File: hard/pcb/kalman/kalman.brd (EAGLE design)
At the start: 84 x 65 mm, 89 parts, among them X1 USB-SMD-NS

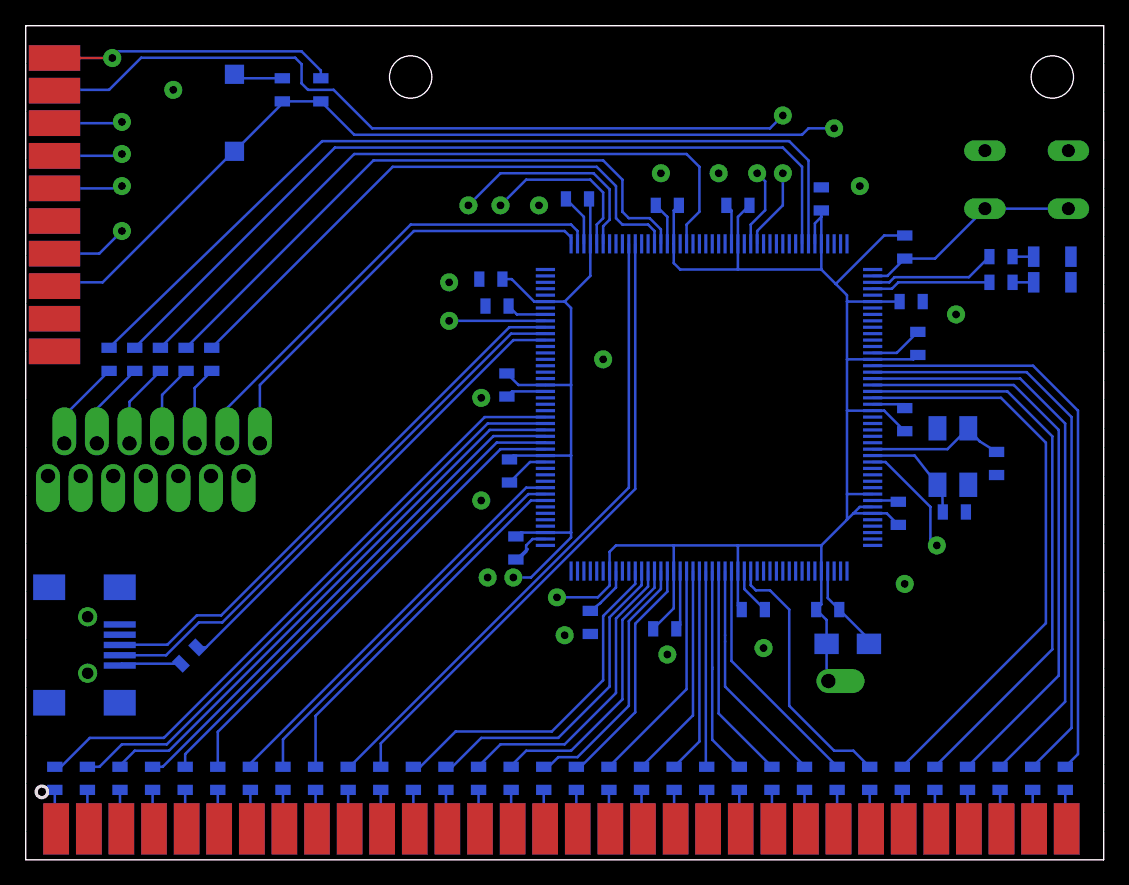
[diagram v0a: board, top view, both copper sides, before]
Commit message: updated kalman tester
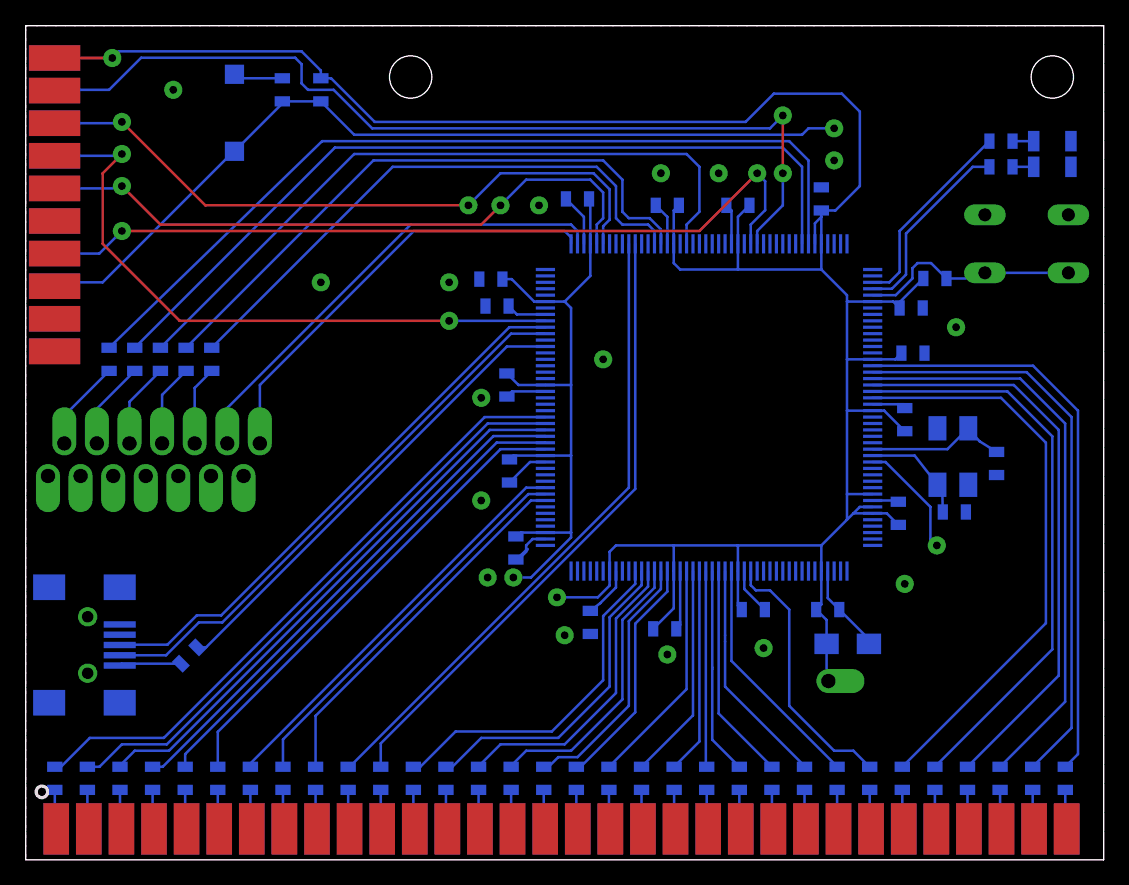
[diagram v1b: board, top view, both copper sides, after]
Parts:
- moved R30 9.00 mm to (76.0, 56.0)
- moved R60 9.00 mm to (76.0, 54.0)
- moved VD1 9.00 mm to (80.0, 56.0)
- moved VD2 9.00 mm to (80.0, 54.0)
- moved S1 5.00 mm to (78.0, 48.0)
- moved R12 3.39 mm to (70.8, 45.3), turned to 0 degrees
- moved C8 0.85 mm to (69.1, 39.5), turned to 0 degrees
- moved C26 0.50 mm to (69.0, 43.0)
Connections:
- net BUTTON: now also U$4.5; no longer U$4.2
- net USB_PRESENT: now also U$4.120; no longer U$4.121
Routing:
- net JTDO: track 12.2 -> 63.6 mm
- net 3.3V: track 209.4 -> 259.0 mm
- net JTMS: track 12.8 -> 49.9 mm
- net JTCK: track 18.7 -> 50.1 mm
- net JTDI: track 22.3 -> 52.0 mm
- net LED_R: track 9.93 -> 15.9 mm
- net LED_G: track 9.31 -> 14.9 mm
- net JTRST: track 67.7 -> 72.2 mm
- net GND: track 49.6 -> 45.4 mm, vias 15 -> 16
